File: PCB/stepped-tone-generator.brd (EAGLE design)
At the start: 80 x 50 mm, 35 parts, among them U1 NE555P, U2 NE556N, U3 CD4017BE

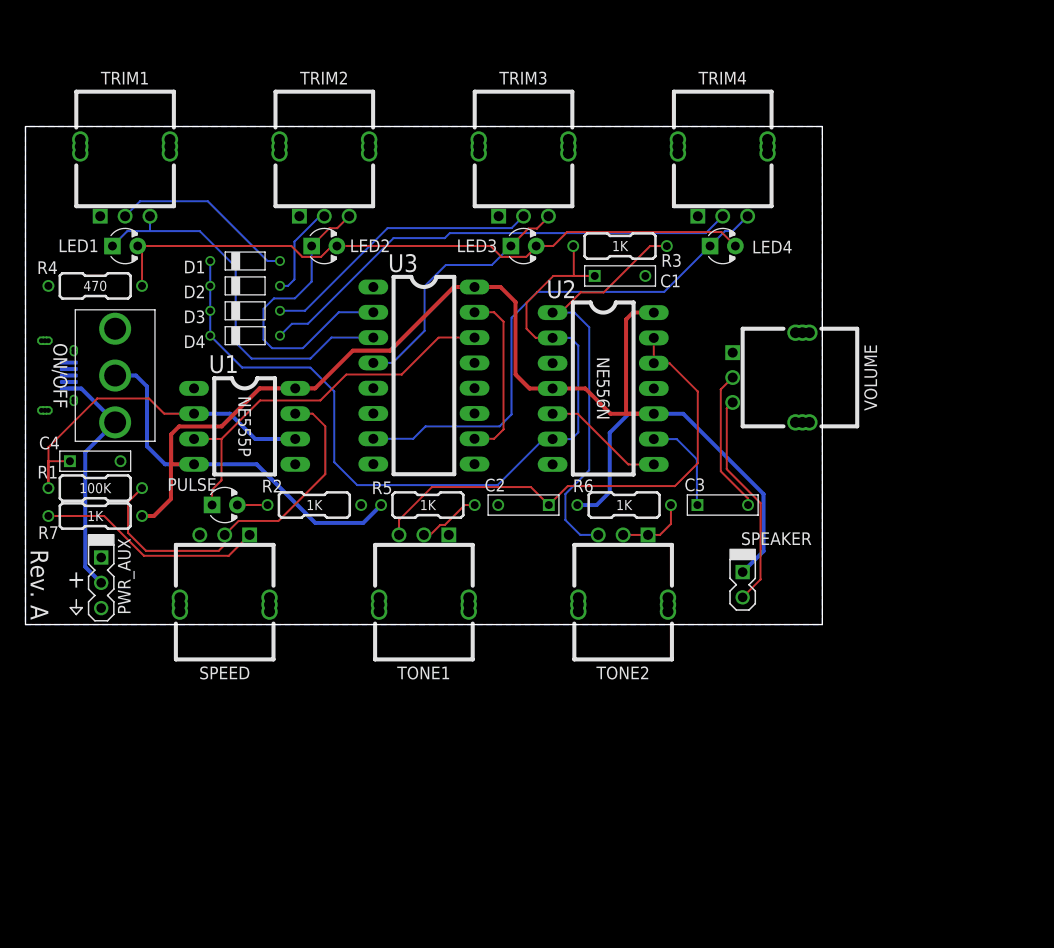
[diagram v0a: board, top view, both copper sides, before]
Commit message: Made PCB larger. Set proper values for pots.
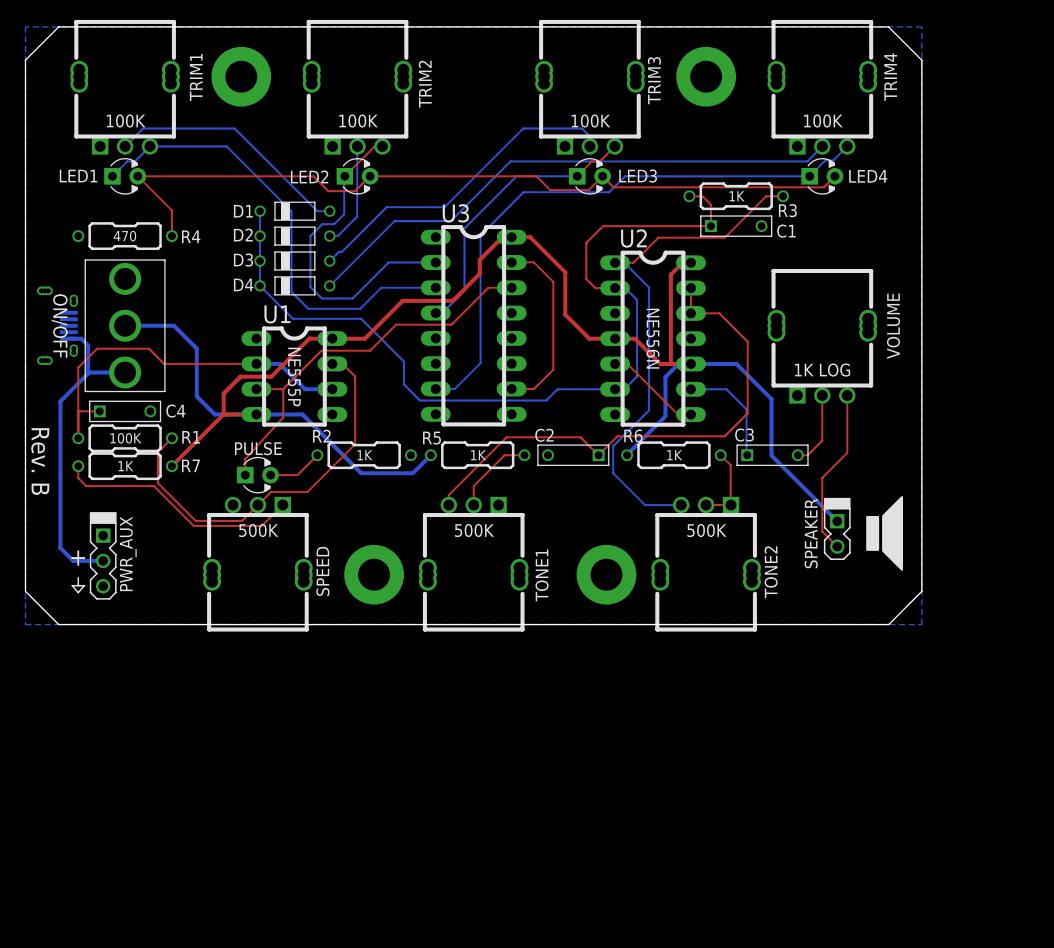
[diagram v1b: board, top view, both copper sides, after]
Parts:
- C1, C2: value 10nF -> 0.01uF
- C4: value 1uF -> 0.01uF
- PWR_AUX: device con-headers:MA03X1 -> con-headers:MA03X1-VT-THD
- VOLUME: value 10K -> 1K LOG
- moved C1 12.7 mm to (71.4, 40.0)
- moved R3 12.7 mm to (71.4, 43.0)
- moved TRIM4 12.2 mm to (80.0, 55.0)
- moved LED4 12.2 mm to (80.0, 45.0)
- moved SPEAKER 10.8 mm to (81.5, 9.10)
- moved LED3 9.67 mm to (56.7, 45.0)
- moved TRIM3 9.67 mm to (56.7, 55.0)
- moved TONE2 8.86 mm to (68.3, 5.00)
- moved LED2 7.75 mm to (33.3, 45.0)
- moved TRIM2 7.75 mm to (33.3, 55.0)
- moved C2 7.07 mm to (55.0, 17.0)
- moved C3 7.07 mm to (75.0, 17.0)
- moved D1 7.07 mm to (27.1, 41.5)
- moved D2 7.07 mm to (27.1, 39.0)
- moved D3 7.07 mm to (27.1, 36.5)
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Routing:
- net N$13: track 67.2 -> 80.7 mm
- net N$8: track 42.8 -> 52.4 mm
- net VIN: track 24.1 -> 32.3 mm
- net N$3: track 38.9 -> 46.1 mm
- net N$21: track 14.4 -> 7.60 mm
- net N$6: track 52.5 -> 58.9 mm
- net N$16: track 18.7 -> 24.7 mm
- net N$19: track 49.4 -> 55.2 mm
- net N$24: track 22.0 -> 16.8 mm
- net N$18: track 28.4 -> 33.0 mm
- net N$11: track 12.3 -> 9.72 mm
- net N$15: track 3.03 -> 5.52 mm
- net N$12: track 37.5 -> 39.9 mm
- net N$4: track 30.5 -> 32.8 mm
- net N$5: track 26.4 -> 28.6 mm
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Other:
- board size 80 x 50 mm -> 90 x 60 mm
- board text added: "Rev. B"
- board text removed: "Rev. A"

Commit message: Added labels for pots.
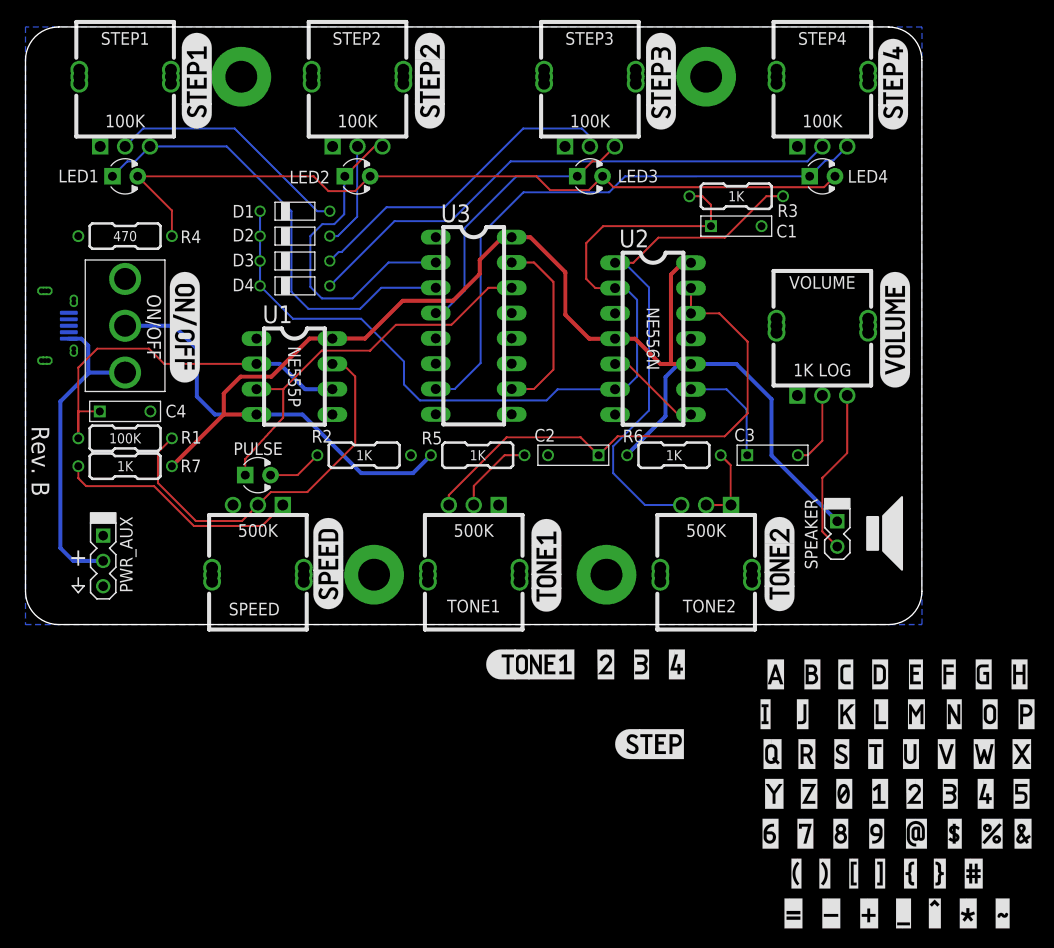
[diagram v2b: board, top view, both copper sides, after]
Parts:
- renumbered TRIM1 to STEP1, TRIM2 to STEP2, TRIM3 to STEP3, TRIM4 to STEP4

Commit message: Stepped tone generator fixes
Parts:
- C4: value 0.01uF -> 1uF
- moved PWR 31.6 mm to (10.0, 0.00), turned to 0 degrees
- moved SPEAKER 2.56 mm to (80.2, 11.3)
- moved PWR_AUX 1.16 mm to (8.07, 7.80), turned to 0 degrees
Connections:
- net N$22: now also SPEED.3; no longer SPEED.1
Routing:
- net VIN: track 32.3 -> 21.5 mm
- net N$22: track 24.6 -> 18.1 mm
- net N$10: track 52.5 -> 49.5 mm
- net VCC: track 165.7 -> 163.2 mm
- net N$11: track 9.72 -> 11.6 mm
- net N$14: track 39.3 -> 37.9 mm
- net N$13: track 80.7 -> 81.9 mm
- net N$24: track 16.8 -> 16.2 mm
- net N$21: track 7.60 -> 7.02 mm
- net N$20: track 87.6 -> 87.0 mm
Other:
- board text added: "+ -"
- board text added: "C i r c u i t M o n k e y"
- board text removed: "CircuitMonkey"
- board text removed: "Rev. B"
